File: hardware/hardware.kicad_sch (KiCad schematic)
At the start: 1 part

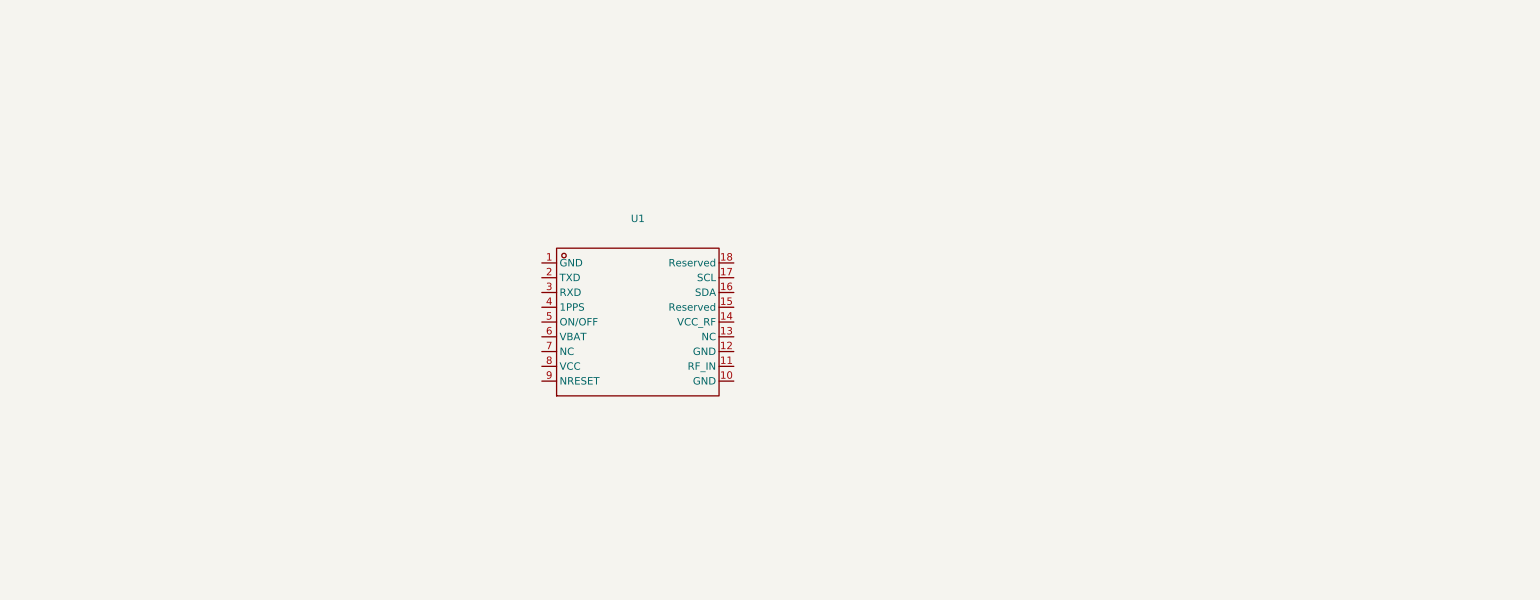
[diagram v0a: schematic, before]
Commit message: first wiring GPS with LNA
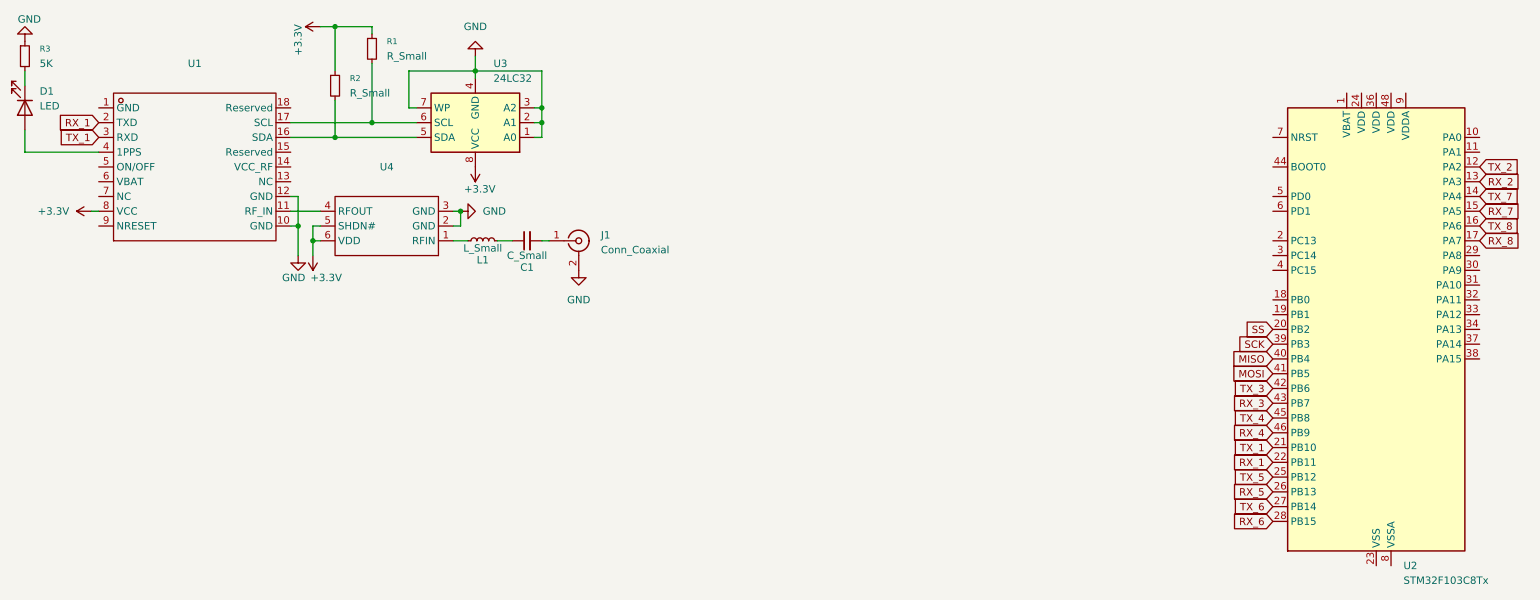
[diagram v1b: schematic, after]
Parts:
- added C1: C_Small, symbol Device:C_Small
- added D1: LED, symbol Device:LED
- added J1: Conn_Coaxial, Connector_Coaxial:U.FL_Molex_MCRF_73412-0110_Vertical, symbol Connector:Conn_Coaxial
- added L1: L_Small, symbol Device:L_Small
- added R1, R2: R_Small, symbol Device:R_Small
- added R3: 5K, symbol Device:R_Small
- added U2: STM32F103C8Tx, Package_QFP:LQFP-48_7x7mm_P0.5mm, symbol MCU_ST_STM32F1:STM32F103C8Tx
- added U3: 24LC32, symbol Memory_EEPROM:24LC32
- added U4: ~, ProLib_pcs_2025-09-27 (2):SOT-23-6_L2.9-W1.6-P0.95-LS2.8-BR, symbol AT2659:AT2659S
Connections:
- net GND: now reaches U1.10 (GND)
- net GND: now also U1.12 (GND), J1.2 (Ext), R3.1, U3.1 (A0), U3.2 (A1), U3.3 (A2), U3.4 (GND), U3.7 (WP), U4.2 (GND), U4.3 (GND)
- net at U1.11 (RF_IN): now also U4.4 (RFOUT)
- net at U1.16 (SDA): now also R2.2, U3.5 (SDA)
- net at U1.17 (SCL): now also R1.2, U3.6 (SCL)
- net RX_1: now reaches U1.2 (TXD)
- net RX_1: now also U2.22 (PB11)
- net TX_1: now reaches U1.3 (RXD)
- net TX_1: now also U2.21 (PB10)
- net at U1.4 (1PPS): now also D1.2 (A)
- net +3.3V: now reaches U1.8 (VCC)
- net +3.3V: now also R1.1, R2.1, U3.8 (VCC), U4.5 (SHDN#), U4.6 (VDD)
- new net: D1.1 (K), R3.2
- new net: C1.2, J1.1 (In)
- new net: L1.1, U4.1 (RFIN)
- new net: C1.1, L1.2
- new net: U2.23 (VSS), U2.35 (VSS), U2.47 (VSS)
- new net MISO: U2.40 (PB4)
- new net MOSI: U2.41 (PB5)
- new net RX_2: U2.13 (PA3)
- new net RX_3: U2.43 (PB7)
- new net RX_4: U2.46 (PB9)
- new net RX_5: U2.26 (PB13)
- new net RX_6: U2.28 (PB15)
- new net RX_7: U2.15 (PA5)
- new net RX_8: U2.17 (PA7)
- new net SCK: U2.39 (PB3)
- new net SS: U2.20 (PB2)
- new net TX_2: U2.12 (PA2)
- new net TX_3: U2.42 (PB6)
- new net TX_4: U2.45 (PB8)
- new net TX_5: U2.25 (PB12)
- new net TX_6: U2.27 (PB14)
- new net TX_7: U2.14 (PA4)
- new net TX_8: U2.16 (PA6)
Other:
- moved on the sheet: U1

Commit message: place all components on pcb
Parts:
- removed C1: C_Small, symbol Device:C_Small
- removed U4: ~, ProLib_pcs_2025-09-27 (2):SOT-23-6_L2.9-W1.6-P0.95-LS2.8-BR, symbol AT2659:AT2659S
- added C10, C9: 20p, Capacitor_SMD:C_0603_1608Metric, symbol Device:C_Small
- added C4, C5, C6, C7: 100n, Capacitor_SMD:C_0603_1608Metric, symbol Device:C_Small
- added C8: 1u, Capacitor_SMD:C_0603_1608Metric, symbol Device:C_Small
- added D10, D4, D5, D6, D7, D8, D9: LED, LED_SMD:LED_0603_1608Metric, symbol Device:LED
- added D2, D3: LED, Diode_SMD:D_0603_1608Metric, symbol Device:LED
- added J10, J4, J5, J6, J7, J8, J9: Conn_Coaxial, Connector_Coaxial:U.FL_Molex_MCRF_73412-0110_Vertical, symbol Connector:Conn_Coaxial
- added J2: BOOT, Connector_PinHeader_2.54mm:PinHeader_2x03_P2.54mm_Vertical, symbol Connector_Generic:Conn_02x03_Top_Bottom
- added J3: SWD, Connector_PinHeader_2.54mm:PinHeader_1x05_P2.54mm_Vertical, symbol Connector_Generic:Conn_01x05
- added L2, L3, L4, L5, L6, L7, L8: L_Small, Inductor_SMD:L_0603_1608Metric, symbol Device:L_Small
- added R10, R14, R17, R21, R24, R27, R30: 5K, Resistor_SMD:R_0603_1608Metric, symbol Device:R_Small
- added R11, R13, R15, R16, R18, R19, R22, R23, R25, R26, R28, R29, R31, R32: R_Small, Resistor_SMD:R_0603_1608Metric, symbol Device:R_Small
- added R20, R6, R7, R8, R9: 10k, Resistor_SMD:R_0603_1608Metric, symbol Device:R_Small
- added R4, R5: 100k, Resistor_SMD:R_0603_1608Metric, symbol Device:R_Small
- added SW1: SW_Push, Button_Switch_SMD:SW_SPST_CK_RS282G05A3, symbol Switch:SW_Push
- added TP1, TP10, TP11, TP12, TP13, TP14, TP15, TP16, TP2, TP3, TP4, TP5, TP6, TP7, TP8, TP9: TestPoint, TestPoint:TestPoint_Pad_D1.5mm, symbol Connector:TestPoint
- added U10, U12, U14, U16, U4, U6, U8: ~, ATGM336H:GPSM-SMD_ATGM336H-TR, symbol ATGM336H:ATGM336H-5N31
- added U11, U13, U15, U17, U5, U7, U9: 24LC32, Package_SO:SOIC-8_3.9x4.9mm_P1.27mm, symbol Memory_EEPROM:24LC32
- added Y2: Crystal_GND24, Crystal:Crystal_SMD_3225-4Pin_3.2x2.5mm, symbol Device:Crystal_GND24
- D1: footprint (none) -> LED_SMD:LED_0603_1608Metric
- L1: footprint (none) -> Inductor_SMD:L_0603_1608Metric
- R1, R2, R3: footprint (none) -> Resistor_SMD:R_0603_1608Metric
- U3: footprint (none) -> Package_SO:SOIC-8_3.9x4.9mm_P1.27mm
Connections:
- net +3.3V: now also U2.1 (VBAT), U2.24 (VDD), U2.36 (VDD), U2.48 (VDD), U2.9 (VDDA), C4.1, C5.1, C6.1, C7.1, J2.1 (Pin_1), J2.2 (Pin_2), J3.5 (Pin_5), R11.1, R13.1, R15.1, R16.1, R18.1, R19.1, R20.1, R22.1, R23.1, R25.1, R26.1, R28.1, R29.1, R31.1, R32.1, R7.1, U10.8 (VCC), U11.8 (VCC), U12.8 (VCC), U13.8 (VCC), U14.8 (VCC), U15.8 (VCC), U16.8 (VCC), U17.8 (VCC), U4.8 (VCC), U5.8 (VCC), U6.8 (VCC), U7.8 (VCC), U8.8 (VCC), U9.8 (VCC)
- net GND: now also U2.23 (VSS), U2.35 (VSS), U2.47 (VSS), U2.8 (VSSA), C10.2, C4.2, C5.2, C6.2, C7.2, C8.2, C9.2, D2.1 (K), D3.1 (K), J10.2 (Ext), J2.5 (Pin_5), J2.6 (Pin_6), J3.1 (Pin_1), J4.2 (Ext), J5.2 (Ext), J6.2 (Ext), J7.2 (Ext), J8.2 (Ext), J9.2 (Ext), R10.1, R14.1, R17.1, R21.1, R24.1, R27.1, R30.1, R6.2, SW1.1, U10.10 (GND), U10.12 (GND), U11.1 (A0), U11.2 (A1), U11.3 (A2), U11.4 (GND), U11.7 (WP), U12.10 (GND), U12.12 (GND), U13.1 (A0), U13.2 (A1), U13.3 (A2), U13.4 (GND), U13.7 (WP), U14.10 (GND), U14.12 (GND), U15.1 (A0), U15.2 (A1), U15.3 (A2), U15.4 (GND), U15.7 (WP), U16.10 (GND), U16.12 (GND), U17.1 (A0), U17.2 (A1), U17.3 (A2), U17.4 (GND), U17.7 (WP), U4.10 (GND), U4.12 (GND), U5.1 (A0), U5.2 (A1), U5.3 (A2), U5.4 (GND), U5.7 (WP), U6.10 (GND), U6.12 (GND), U7.1 (A0), U7.2 (A1), U7.3 (A2), U7.4 (GND), U7.7 (WP), U8.10 (GND), U8.12 (GND), U9.1 (A0), U9.2 (A1), U9.3 (A2), U9.4 (GND), U9.7 (WP), Y2.1, Y2.3
- net RX_1: now also TP1.1
- net RX_2: now also TP3.1, U4.2 (TXD)
- net RX_3: now also TP5.1, U6.2 (TXD)
- net RX_4: now also TP7.1, U8.2 (TXD)
- net RX_5: now also TP9.1, U10.2 (TXD)
- net RX_6: now also TP11.1, U12.2 (TXD)
- net RX_7: now also TP13.1, U14.2 (TXD)
- net RX_8: now also TP15.1, U16.2 (TXD)
- net SS: now also U2.19 (PB1); no longer U2.20 (PB2)
- net TX_1: now also TP2.1
- net TX_2: now also TP4.1, U4.3 (RXD)
- net TX_3: now also TP6.1, U6.3 (RXD)
- net TX_4: now also TP8.1, U8.3 (RXD)
- net TX_5: now also TP10.1, U10.3 (RXD)
- net TX_6: now also TP12.1, U12.3 (RXD)
- net TX_7: now also TP14.1, U14.3 (RXD)
- net TX_8: now also TP16.1, U16.3 (RXD)
- net at J1.1 (In): now also U1.11 (RF_IN), L2.1
- net at L1.1: now also J4.1 (In), U4.11 (RF_IN)
- net at U1.14 (VCC_RF): now also L2.2
- net at L1.2: now also U4.14 (VCC_RF)
- net OSIN: now reaches U2.2 (PC13)
- net OSIN: now also C9.1, Y2.2
- net OSOUT: now reaches U2.3 (PC14)
- net OSOUT: now also C10.1, Y2.4
- net SWDIO: now reaches U2.34 (PA13)
- net SWDIO: now also J3.4 (Pin_4), R6.1
- net SWCLK: now reaches U2.37 (PA14)
- net SWCLK: now also J3.3 (Pin_3), R7.2
- net BOOT0: now reaches U2.44 (BOOT0)
- net BOOT0: now also R4.1
- net RST: now reaches U2.7 (NRST)
- new net: R15.2, U6.16 (SDA), U7.5 (SDA)
- new net: R16.2, U6.17 (SCL), U7.6 (SCL)
- new net: R31.2, U16.16 (SDA), U17.5 (SDA)
- new net: J10.1 (In), L8.1, U16.11 (RF_IN)
- new net: L8.2, U16.14 (VCC_RF)
- new net: R32.2, U16.17 (SCL), U17.6 (SCL)
- new net: D10.2 (A), U16.4 (1PPS)
- new net: D3.2 (A), R9.2
- new net: R19.2, U8.17 (SCL), U9.6 (SCL)
- new net: R22.2, U10.16 (SDA), U11.5 (SDA)
- new net: R23.2, U10.17 (SCL), U11.6 (SCL)
- new net: J5.1 (In), L3.1, U6.11 (RF_IN)
- new net: D9.1 (K), R27.2
- new net: D9.2 (A), U14.4 (1PPS)
- new net: J6.1 (In), L4.1, U8.11 (RF_IN)
- new net: L4.2, U8.14 (VCC_RF)
- new net: R18.2, U8.16 (SDA), U9.5 (SDA)
- new net: D6.2 (A), U8.4 (1PPS)
- new net: R25.2, U12.16 (SDA), U13.5 (SDA)
- new net: J9.1 (In), L7.1, U14.11 (RF_IN)
- new net: L7.2, U14.14 (VCC_RF)
- new net: D6.1 (K), R17.2
- new net: J8.1 (In), L6.1, U12.11 (RF_IN)
- new net: L6.2, U12.14 (VCC_RF)
- new net: R26.2, U12.17 (SCL), U13.6 (SCL)
- new net: D8.2 (A), U12.4 (1PPS)
- new net: D5.1 (K), R14.2
- new net: D5.2 (A), U6.4 (1PPS)
- new net: D10.1 (K), R30.2
- new net: R11.2, U4.16 (SDA), U5.5 (SDA)
- new net: D4.1 (K), R10.2
- new net: R13.2, U4.17 (SCL), U5.6 (SCL)
- new net: D4.2 (A), U4.4 (1PPS)
- new net: L3.2, U6.14 (VCC_RF)
- new net: D7.1 (K), R21.2
- new net: D7.2 (A), U10.4 (1PPS)
- new net: R28.2, U14.16 (SDA), U15.5 (SDA)
- new net: R29.2, U14.17 (SCL), U15.6 (SCL)
- new net: D8.1 (K), R24.2
- new net: J7.1 (In), L5.1, U10.11 (RF_IN)
- new net: L5.2, U10.14 (VCC_RF)
- new net: D2.2 (A), R8.2
- new net: J2.4 (Pin_4), R5.1
- new net: J2.3 (Pin_3), R4.2
- new net BOOT1: R5.2, U2.20 (PB2)
- new net LED1: R8.1
- new net LED2: R9.1
- new net RESET: C8.1, J3.2 (Pin_2), R20.2, SW1.2
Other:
- moved on the sheet: J1, U2

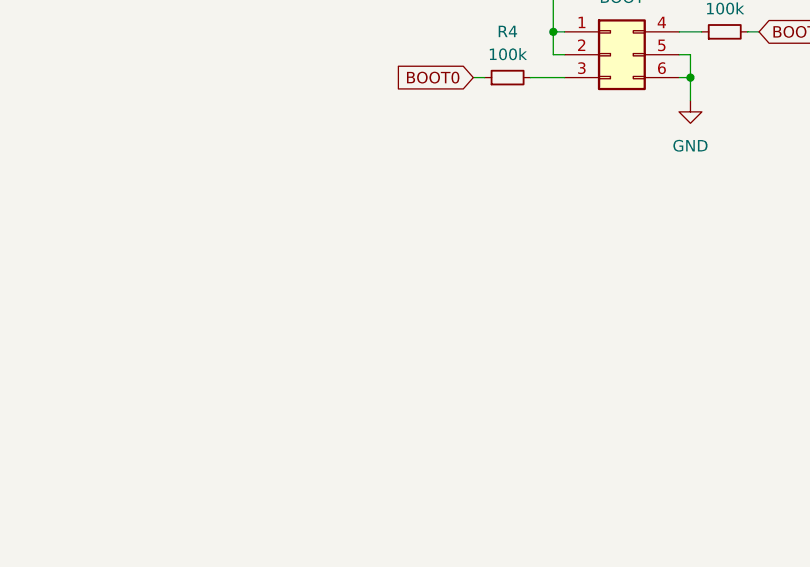
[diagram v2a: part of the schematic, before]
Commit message: add power and comm connector
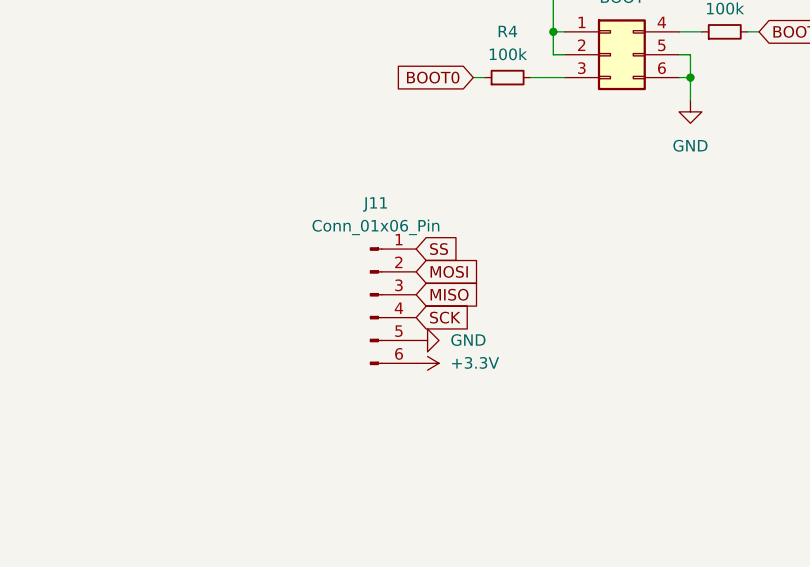
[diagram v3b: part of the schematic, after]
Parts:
- added J11: Conn_01x06_Pin, symbol Connector:Conn_01x06_Pin
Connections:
- net +3.3V: now also J11.6 (Pin_6)
- net GND: now also J11.5 (Pin_5)
- net MISO: now also J11.3 (Pin_3)
- net MOSI: now also J11.2 (Pin_2)
- net SCK: now also J11.4 (Pin_4)
- net SS: now also J11.1 (Pin_1)

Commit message: full wiring pcb
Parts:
- removed R4, R5: 100k, Resistor_SMD:R_0603_1608Metric, symbol Device:R_Small
- J11: footprint (none) -> Connector_JST:JST_SH_BM06B-SRSS-TB_1x06-1MP_P1.00mm_Vertical
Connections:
- net RST is gone; now on net RESET: U2.7 (NRST)
- net BOOT0: now also J2.3 (Pin_3)
- net BOOT1: now also J2.4 (Pin_4)
- net LED1: now also U2.30 (PA9)
- net LED2: now also U2.29 (PA8)
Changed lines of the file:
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@@
 	(wire
 		(pts
-			(xy 341.63 147.32) (xy 340.36 147.32)
-		)
-		(stroke
-			(width 0)
-			(type default)
-		)
-	)
-	(wire
-		(pts
 			(xy 92.71 21.59) (xy 92.71 24.13)
 		)
@@
 	(wire
 		(pts
-			(xy 332.74 147.32) (xy 335.28 147.32)
+			(xy 332.74 147.32) (xy 341.63 147.32)
 		)
 		(stroke
@@
 	(wire
 		(pts
-			(xy 309.88 152.4) (xy 311.15 152.4)
+			(xy 309.88 152.4) (xy 320.04 152.4)
 		)
 		(stroke
@@
 	(wire
 		(pts
-			(xy 316.23 152.4) (xy 320.04 152.4)
-		)
-		(stroke
-			(width 0)
-			(type default)
-		)
-	)
-	(wire
-		(pts
 			(xy 370.84 135.89) (xy 375.92 135.89)
 		)
@@
 		)
 	)
+	(global_label "RESET"
+		(shape input)
+		(at 350.52 36.83 180)
+		(fields_autoplaced yes)
+		(effects
+			(font
+				(size 1.27 1.27)
+			)
+			(justify right)
+		)
+		(property "Intersheetrefs" "${INTERSHEET_REFS}"
+			(at 341.7897 36.83 0)
+			(effects
+				(font
+					(size 1.27 1.27)
+				)
+				(justify right)
+				(hide yes)
+			)
+		)
+	)
 	(global_label "RX_2"
 		(shape input)
@@
 		)
 	)
-	(global_label "RST"
+	(global_label "RX_2"
 		(shape input)
-		(at 350.52 36.83 180)
+		(at 24.13 81.28 180)
 		(fields_autoplaced yes)
 		(effects
@@
 		)
 		(property "Intersheetrefs" "${INTERSHEET_REFS}"
-			(at 344.0877 36.83 0)
+			(at 16.4882 81.28 0)
 			(effects
 				(font
@@
 		)
 	)
-	(global_label "RX_2"
+	(global_label "TX_6"
 		(shape input)
-		(at 24.13 81.28 180)
+		(at 350.52 100.33 180)
 		(fields_autoplaced yes)
 		(effects
@@
 		)
 		(property "Intersheetrefs" "${INTERSHEET_REFS}"
-			(at 16.4882 81.28 0)
+			(at 343.1806 100.33 0)
 			(effects
 				(font
@@
 		)
 	)
-	(global_label "TX_6"
+	(global_label "RX_4"
 		(shape input)
-		(at 350.52 100.33 180)
+		(at 350.52 87.63 180)
 		(fields_autoplaced yes)
 		(effects
@@
 		)
 		(property "Intersheetrefs" "${INTERSHEET_REFS}"
-			(at 343.1806 100.33 0)
+			(at 342.8782 87.63 0)
 			(effects
 				(font
@@
 		)
 	)
-	(global_label "RX_4"
+	(global_label "LED2"
 		(shape input)
-		(at 350.52 87.63 180)
+		(at 386.08 57.15 0)
 		(fields_autoplaced yes)
 		(effects
@@
 				(size 1.27 1.27)
 			)
-			(justify right)
+			(justify left)
 		)
 		(property "Intersheetrefs" "${INTERSHEET_REFS}"
-			(at 342.8782 87.63 0)
+			(at 393.7218 57.15 0)
 			(effects
 				(font
 					(size 1.27 1.27)
 				)
-				(justify right)
+				(justify left)
 				(hide yes)
 			)
@@
 		)
 	)
+	(global_label "LED1"
+		(shape input)
+		(at 386.08 59.69 0)
+		(fields_autoplaced yes)
+		(effects
+			(font
+				(size 1.27 1.27)
+			)
+			(justify left)
+		)
+		(property "Intersheetrefs" "${INTERSHEET_REFS}"
+			(at 393.7218 59.69 0)
+			(effects
+				(font
+					(size 1.27 1.27)
+				)
+				(justify left)
+				(hide yes)
+			)
+		)
+	)
 	(global_label "TX_7"
 		(shape input)
@@
 			)
 		)
-		(property "Footprint" ""
+		(property "Footprint" "Connector_JST:JST_SH_BM06B-SRSS-TB_1x06-1MP_P1.00mm_Vertical"
 			(at 298.45 176.53 0)
 			(effects
@@
 	(symbol
 		(lib_id "Device:R_Small")
-		(at 337.82 147.32 90)
-		(unit 1)
-		(exclude_from_sim no)
-		(in_bom yes)
-		(on_board yes)
-		(dnp no)
-		(fields_autoplaced yes)
-		(property "Reference" "R5"
-			(at 337.82 142.24 90)
-			(effects
-				(font
-					(size 1.27 1.27)
-				)
-			)
-		)
-		(property "Value" "100k"
-			(at 337.82 144.78 90)
-			(effects
-				(font
-					(size 1.27 1.27)
-				)
-			)
-		)
-		(property "Footprint" "Resistor_SMD:R_0603_1608Metric"
-			(at 337.82 147.32 0)
-			(effects
-				(font
-					(size 1.27 1.27)
-				)
-				(hide yes)
-			)
-		)
-		(property "Datasheet" "~"
-			(at 337.82 147.32 0)
-			(effects
-				(font
-					(size 1.27 1.27)
-				)
-				(hide yes)
-			)
-		)
-		(property "Description" ""
-			(at 337.82 147.32 0)
-			(effects
-				(font
-					(size 1.27 1.27)
-				)
-				(hide yes)
-			)
-		)
-		(pin "1"
-		)
-		(pin "2"
-		)
-		(instances
-			(project "hardware"
-				(path "/f3b7aafd-186b-4744-9db2-48ed432acba7"
-					(reference "R5")
-					(unit 1)
-				)
-			)
-		)
-	)
-	(symbol
-		(lib_id "Device:R_Small")
 		(at 316.23 105.41 0)
 		(unit 1)
@@
 					(unit 1)
 				)
-			)
-		)
-	)
-	(symbol
-		(lib_id "Device:R_Small")
-		(at 313.69 152.4 90)
-		(unit 1)
-		(exclude_from_sim no)
-		(in_bom yes)
-		(on_board yes)
-		(dnp no)
-		(fields_autoplaced yes)
-		(property "Reference" "R4"
-			(at 313.69 147.32 90)
-			(effects
-				(font
-					(size 1.27 1.27)
-				)
-			)
-		)
-		(property "Value" "100k"
-			(at 313.69 149.86 90)
-			(effects
-				(font
-					(size 1.27 1.27)
-				)
-			)
-		)
-		(property "Footprint" "Resistor_SMD:R_0603_1608Metric"
-			(at 313.69 152.4 0)
-			(effects
-				(font
-					(size 1.27 1.27)
-				)
-				(hide yes)
-			)
-		)
-		(property "Datasheet" "~"
-			(at 313.69 152.4 0)
-			(effects
-				(font
-					(size 1.27 1.27)
-				)
-				(hide yes)
-			)
-		)
-		(property "Description" ""
-			(at 313.69 152.4 0)
-			(effects
-				(font
-					(size 1.27 1.27)
-				)
-				(hide yes)
-			)
-		)
-		(pin "1"
-		)
-		(pin "2"
-		)
-		(instances
-			(project "hardware"
-				(path "/f3b7aafd-186b-4744-9db2-48ed432acba7"
-					(reference "R4")
-					(unit 1)
-				)

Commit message: add connector step
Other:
- company: (none) -> RMINGON
- title: (none) -> GPS_ARRAY_FUSION
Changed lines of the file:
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@@
 	(generator_version "9.0")
 	(paper "A3")
+	(title_block
+		(title "GPS_ARRAY_FUSION")
+		(date "2025-09-28")
+		(rev "0.1")
+		(company "RMINGON")
+	)
 	(junction
 		(at 195.58 110.49)

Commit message: fix gnss ground module
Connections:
- net GND: now also U1.1 (GND), U10.1 (GND), U12.1 (GND), U14.1 (GND), U16.1 (GND), U4.1 (GND), U6.1 (GND), U8.1 (GND)
